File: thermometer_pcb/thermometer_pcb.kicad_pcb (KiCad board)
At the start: 2 copper layers, 76.6 x 49 mm, 23 parts, among them J1 POWER_IN, J2 TC_IN, J3 EXT_DS1, J4 EXT_DS2, J5 DISP, J6 Conn_01x02, J7 SPI, J8 I2C, J9 ENC, Q1 PN2222A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

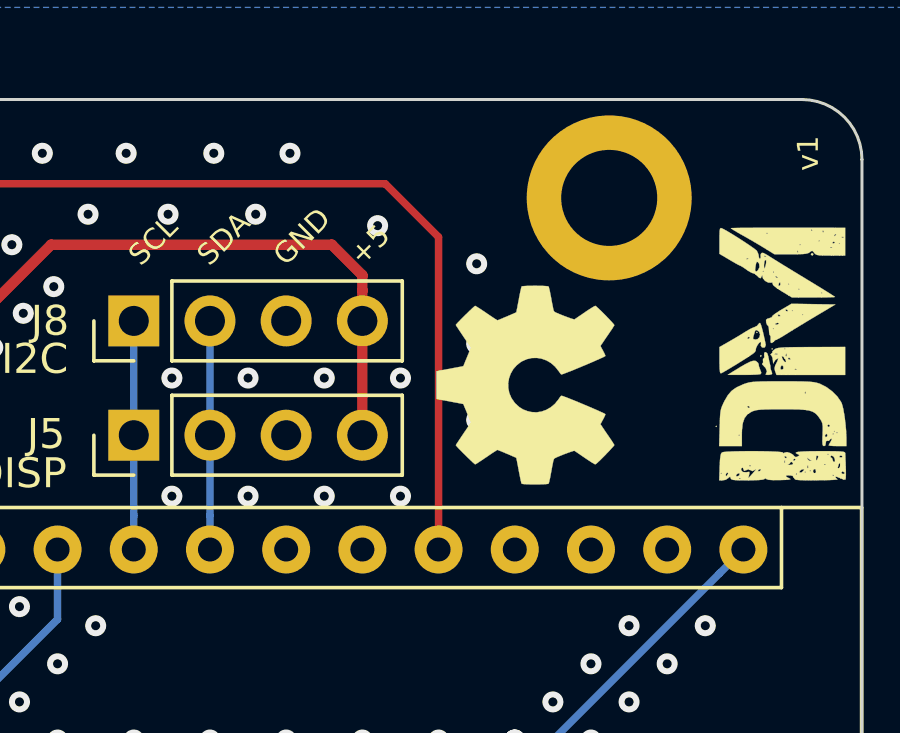
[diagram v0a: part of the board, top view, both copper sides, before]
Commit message: pcb: use A0 for encoders switch
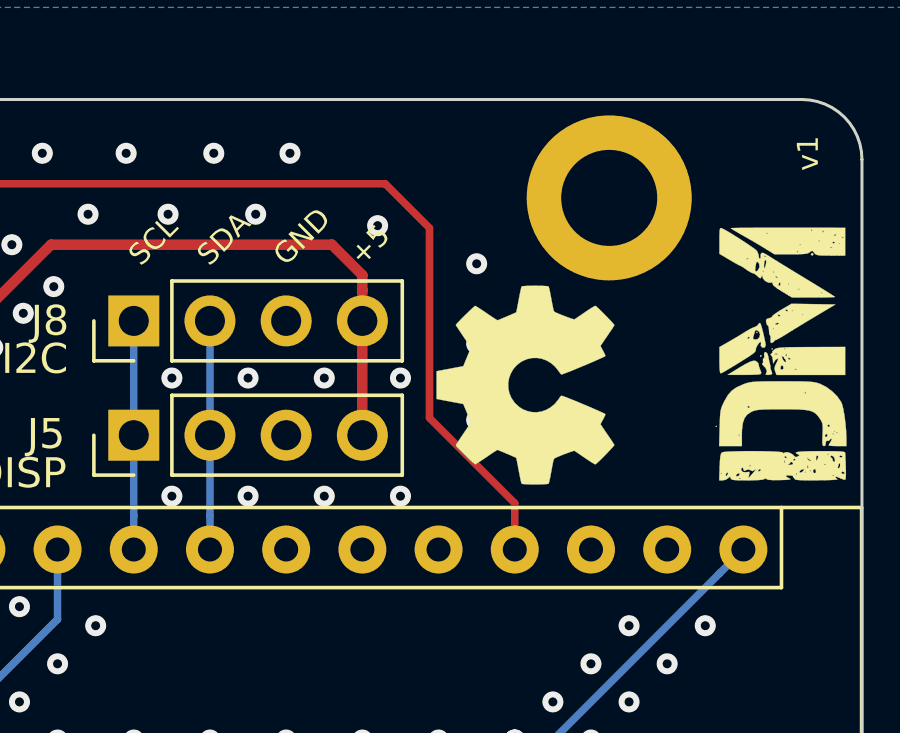
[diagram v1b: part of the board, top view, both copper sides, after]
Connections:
- A1 pad 19: (no net) -> /A0
- A1 pad 20: /A1 -> (no net)
- J9 pad 3: /A1 -> /A0
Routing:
- net /A0: track 0.00 -> 41.4 mm
- net /A1: track 40.4 -> 0.00 mm

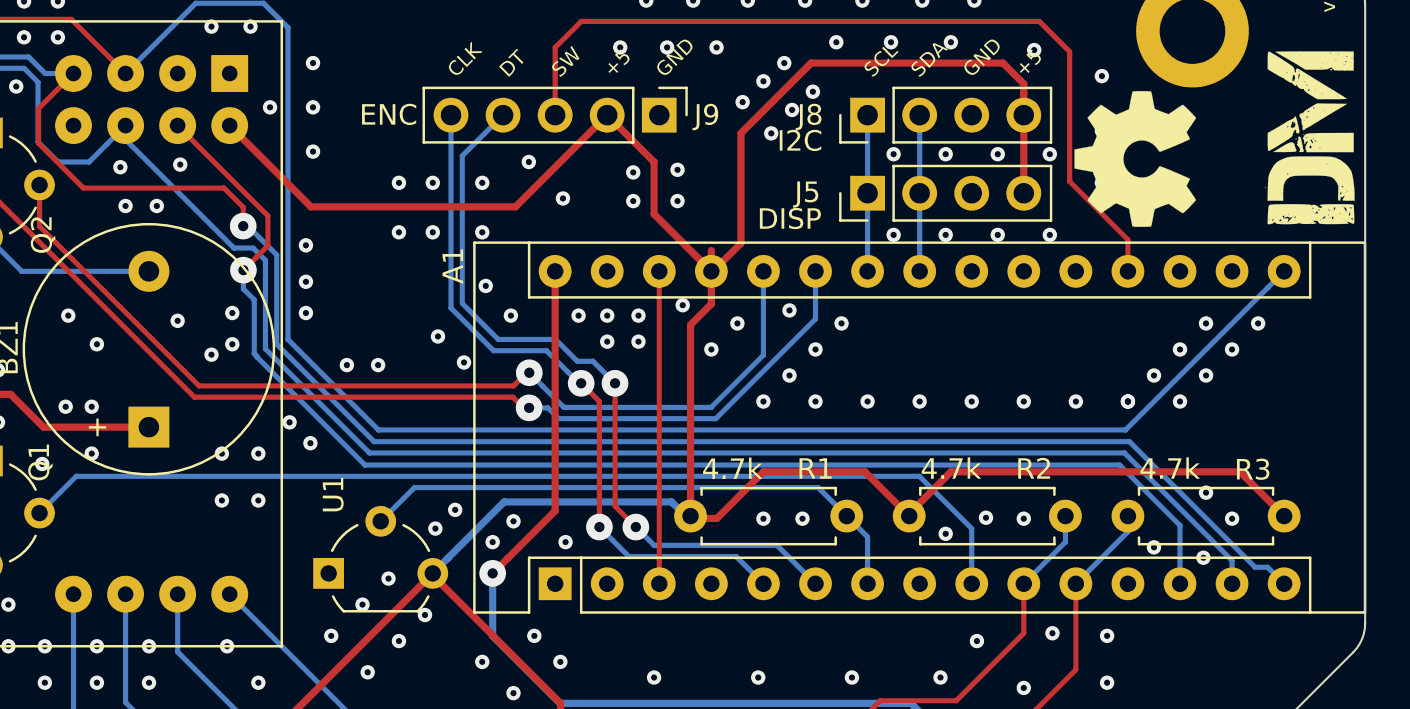
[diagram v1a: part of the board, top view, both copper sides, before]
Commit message: pcb: use A1 for external SPI CS
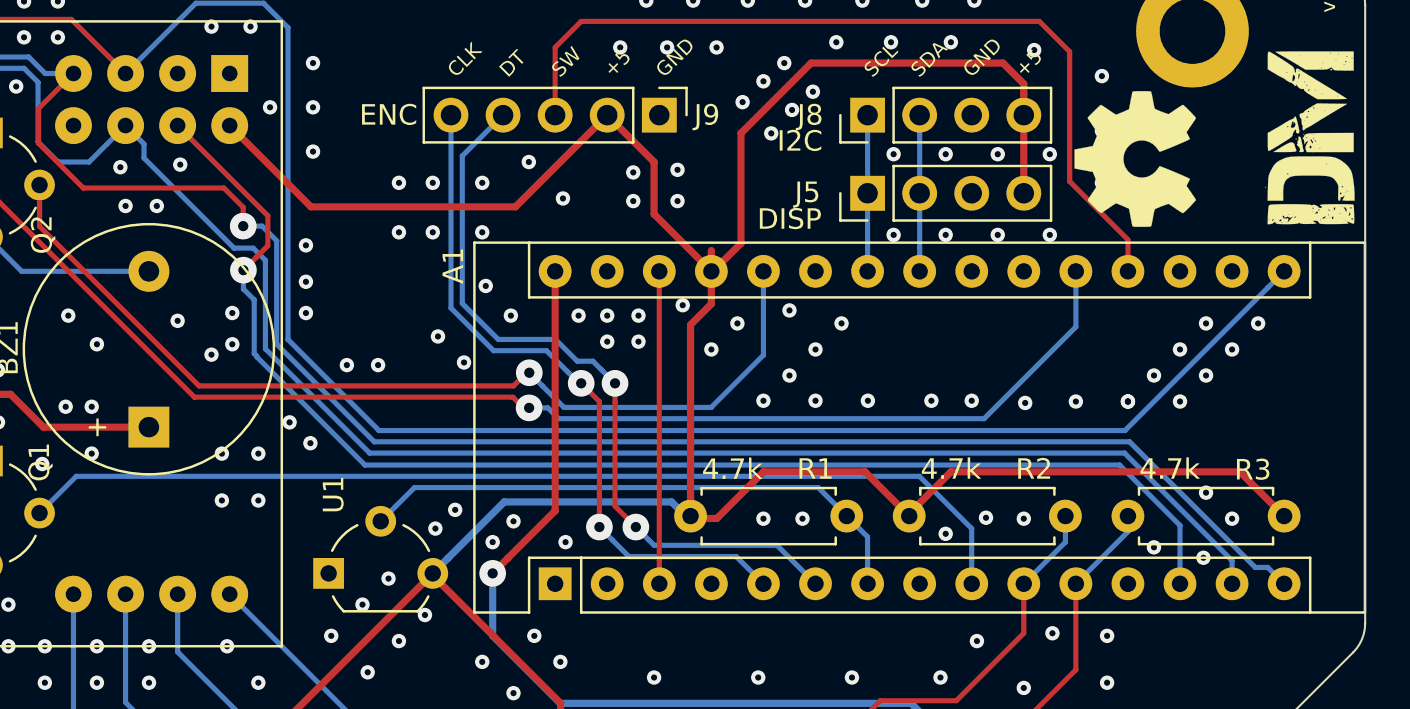
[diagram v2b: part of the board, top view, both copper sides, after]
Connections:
- A1 pad 20: (no net) -> /A1
- A1 pad 25: /A6 -> (no net)
- J7 pad 6: /A6 -> /A1
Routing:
- net /A1: track 0.00 -> 67.8 mm, vias 0 -> 1
- net /A6: track 54.8 -> 0.00 mm, vias 1 -> 0

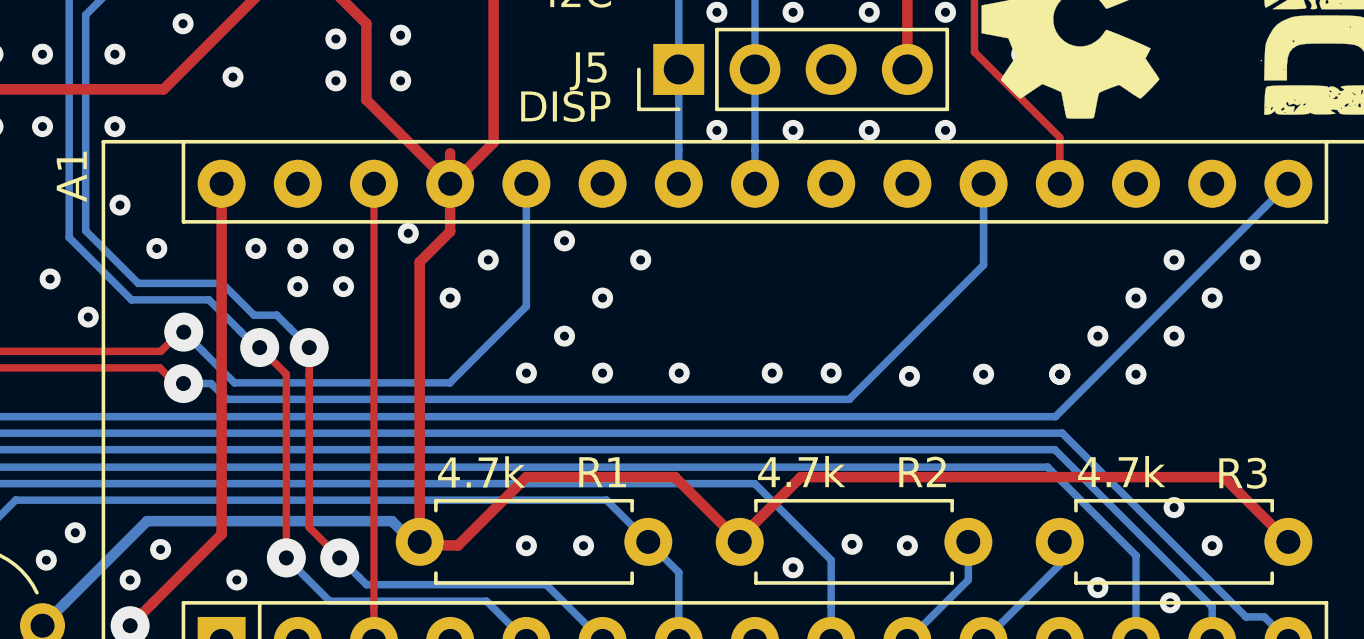
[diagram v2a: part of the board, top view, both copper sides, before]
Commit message: pcb: use A2 for buzzer
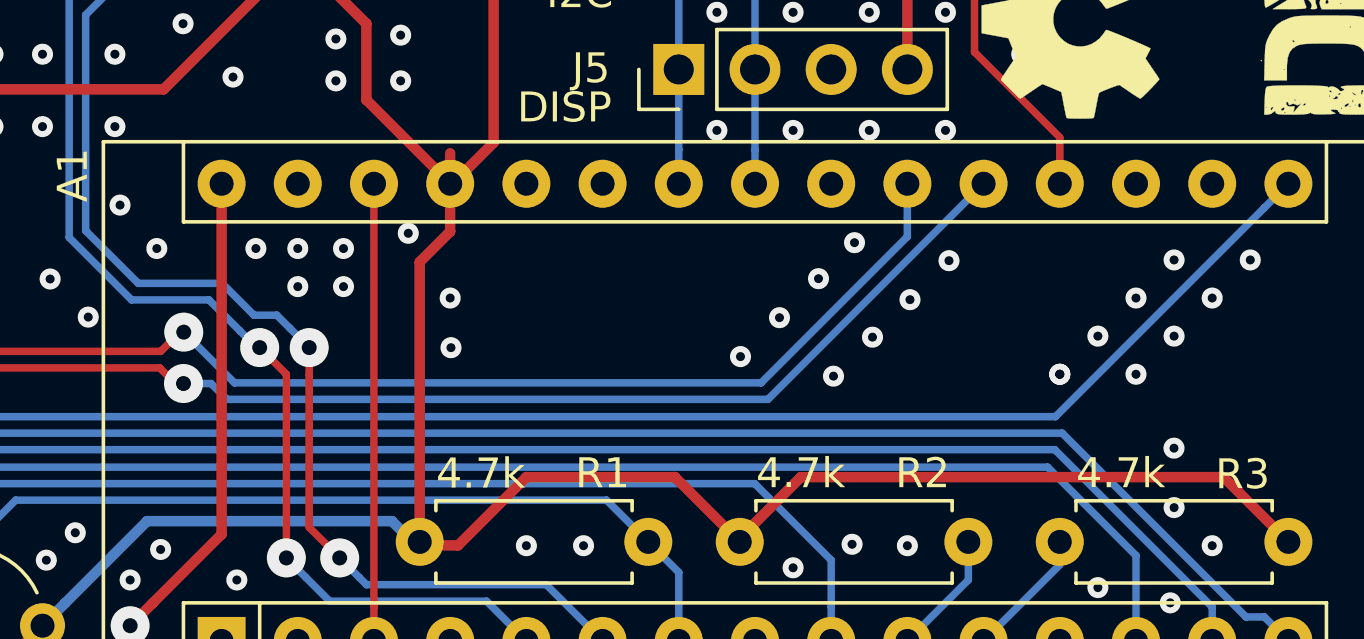
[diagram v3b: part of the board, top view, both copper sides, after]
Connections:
- A1 pad 21: (no net) -> /A2
- A1 pad 26: /A7 -> (no net)
- Q2 pad 2: /A7 -> /A2
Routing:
- net /A2: track 0.00 -> 58.0 mm, vias 0 -> 1
- net /A7: track 46.7 -> 0.00 mm, vias 1 -> 0
- net /A1: track 67.8 -> 66.2 mm
- net GND: vias 203 -> 201

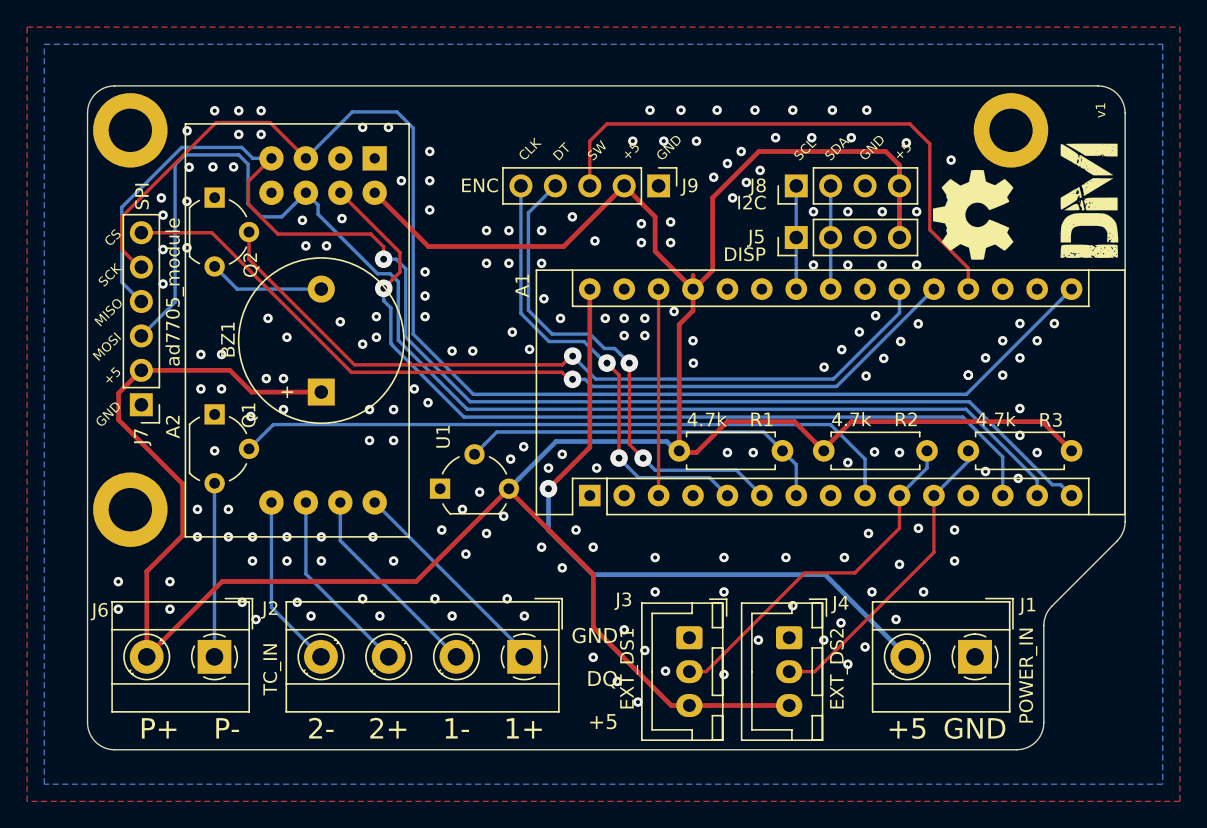
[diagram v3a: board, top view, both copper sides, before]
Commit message: pcb: move some tracks to back layer
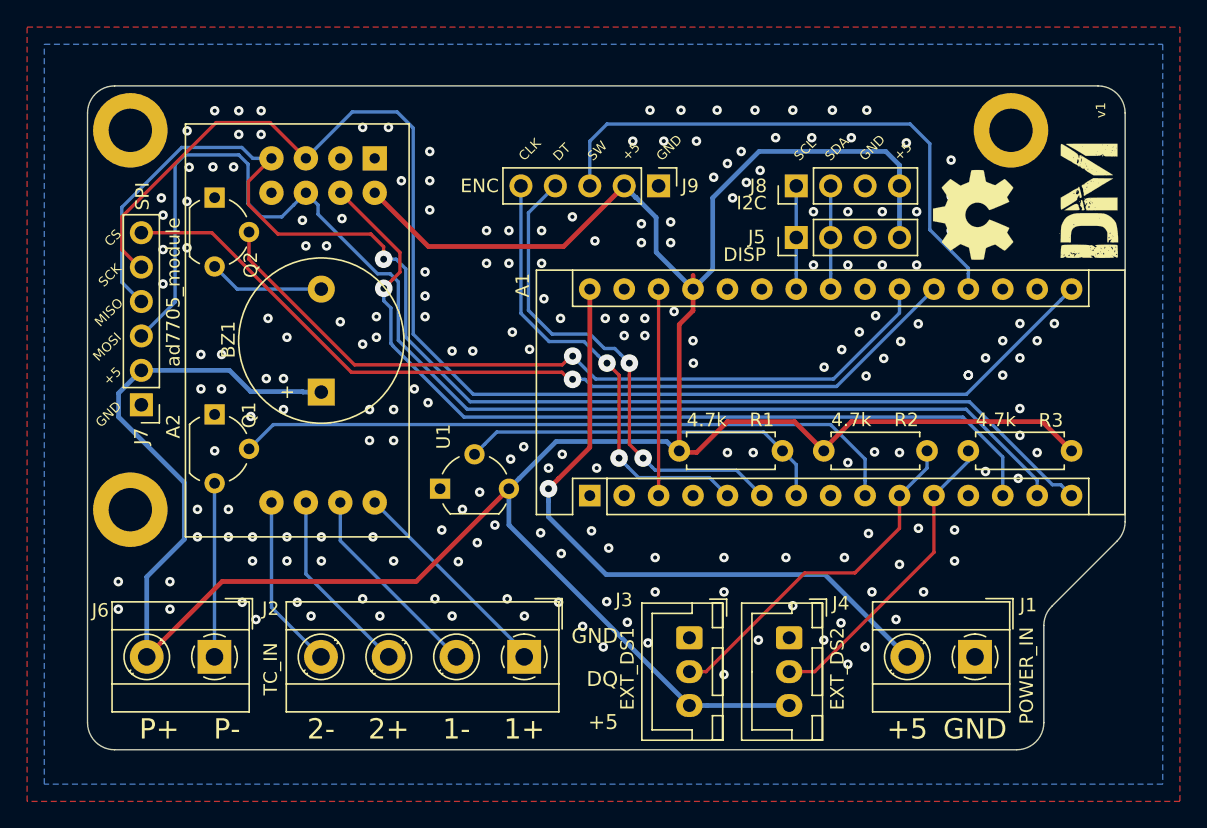
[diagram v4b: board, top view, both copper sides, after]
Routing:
- net +5V: track 220.5 -> 219.9 mm
- net /Vin: track 49.4 -> 48.8 mm

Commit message: pcb: version v2
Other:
- board text added: "v2"
- board text removed: "v1"
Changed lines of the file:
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@@
       (net 1 "GND") (zone_connect 2))
   )
-  (gr_text "v1" (at 220.427677 45.810604 90) (layer "F.SilkS")
+  (gr_text "v2" (at 220.427677 45.810604 90) (layer "F.SilkS")
     (effects (font (size 0.7 0.7) (thickness 0.1)))
   )

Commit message: pcb: align some tracks
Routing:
- net /12(MISO): track 98.0 -> 97.1 mm

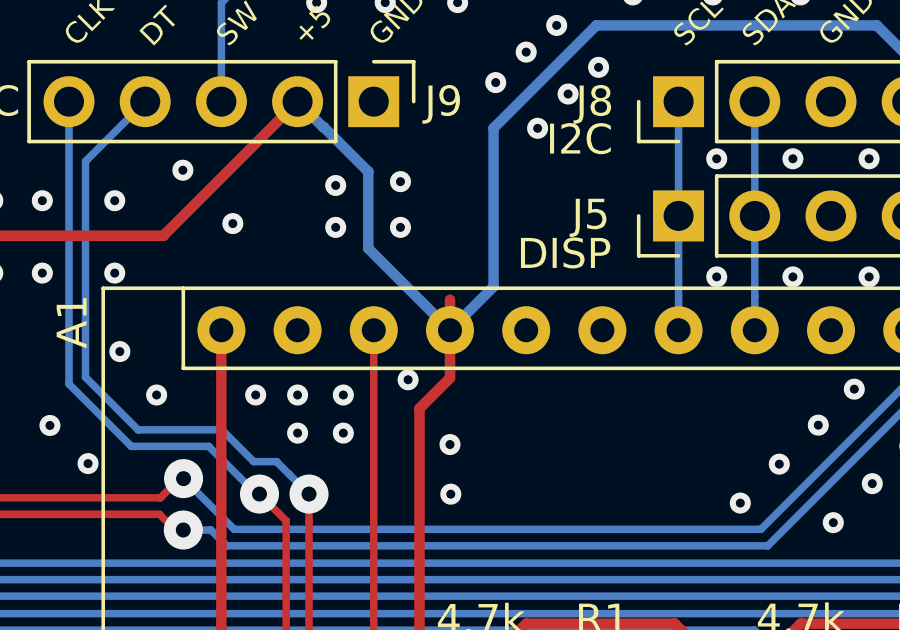
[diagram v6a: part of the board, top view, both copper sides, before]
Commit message: pcb: remove wrong track segment
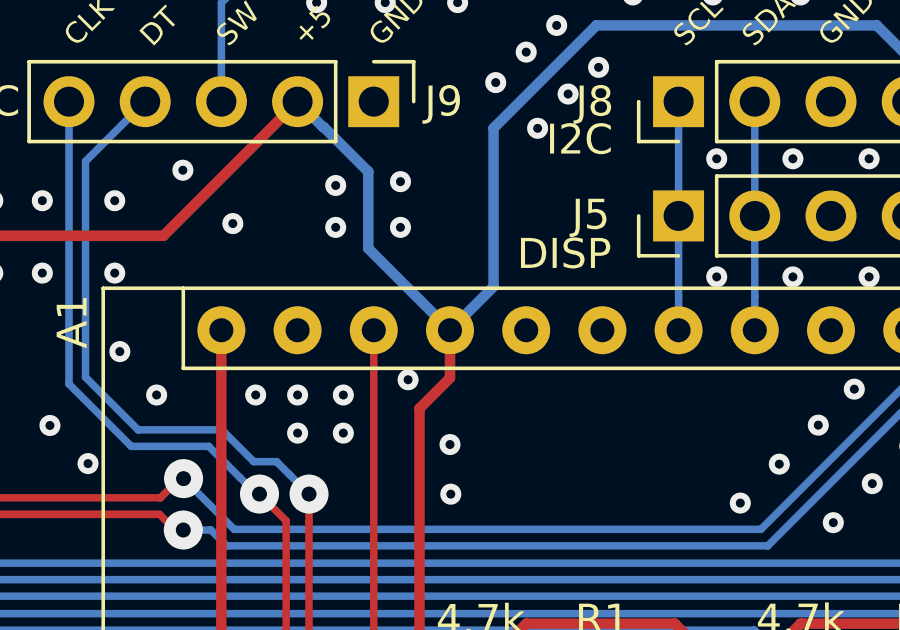
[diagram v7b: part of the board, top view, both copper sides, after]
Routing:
- net +5V: track 219.9 -> 218.9 mm
